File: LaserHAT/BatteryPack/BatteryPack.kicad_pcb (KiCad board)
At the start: 2 copper layers, 100 x 96 mm, 101 parts, among them J1 USB-C PD 20V in, J3 OUT +V/0V/-V + link, J4 LINK from lower pack, Q1 AO3401A, Q10 AO3400A, Q2 AO3401A, Q3 AO3400A, Q4 AO3401A, Q5 AO3400A, Q6 AO3401A, Q7 AO3400A, Q8 AO3400A, Q9 AO3400A, SW1 MTS-203 RUN/OFF/CHG, U1 LM393DR2G, U2 LM393DR2G, U3 CJ431, U4 CH224A, U5 CN3704, U6 HY2213-BB3A, U7 HY2213-BB3A, U8 HY2213-BB3A, U9 HY2213-BB3A

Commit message: BatteryPack: all four cells the same way round, 4 mm polarity marks under each cell
The cells alternated direction in the first routing (short series links);
the user prefers one orientation to avoid insertion errors.  tools/place.py
now puts the - clip (odd BCn) on the left and the + clip on the right in all
four rows and draws 4 mm "-" / "+" silk strokes under each cell body, in
addition to the small marks beside the clips.  The cell-area copper (C1-C3,
GND and +BAT west of the strip) was ripped up and rerouted with Freerouting;
the electronics strip kept its routing.  DRC 0 violations / 0 unconnected,
path_check / sync_check 0; fab outputs and renders regenerated.

Co-Authored-By: Claude Fable 5.1 <noreply@anthropic.com>
Claude-Session: https://claude.ai/code/session_018vgLizGzYPynnY93ajvoVA
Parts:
- moved BC1 48.0 mm to (11.0, 17.0), turned to 0 degrees
- moved BC2 48.0 mm to (59.0, 17.0), turned to 180 degrees
- moved BC5 48.0 mm to (11.0, 57.0), turned to 0 degrees
- moved BC6 48.0 mm to (59.0, 57.0), turned to 180 degrees
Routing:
- net GND: track 283.1 -> 358.7 mm
- net /C2: track 104.3 -> 145.3 mm, vias 2 -> 3
- net /C1: track 124.2 -> 162.1 mm
- net /C3: track 113.6 -> 129.4 mm
- net +BAT: track 166.9 -> 164.9 mm

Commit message: BatteryPack: LCSC codes on the board footprints, JLC model strings as values
A BOM made from the PCB with the Fabrication Toolkit had no part numbers,
because the footprints carried none; JLC then matched by Comment and failed on
the parts with descriptive values (C5, F1, J1, J3, J4, SW1).

- sch_engine.py writes the code into every symbol as "LCSC Part #" (the field
  the Fabrication Toolkit reads) instead of "LCSC"; mounting holes are out of
  the BOM
- new tools/stamp_fields.py stamps the same field (hidden, F.Fab) into every
  footprint, syncs the Values and excludes H1-H4 from BOM and position files
- values of the toggle, PTC, LEDs, USB-C, PH-4 headers, inductor and NTC are
  now JLC's model strings so the Comment matches; J3/J4 roles noted as text
- schematic regenerated (netcheck OK, ERC 0), path/sync checks 0, DRC 0/0,
  fab outputs and PDF regenerated; all codes verified against JLC (toggle
  stock 192)

Co-Authored-By: Claude Fable 5.1 <noreply@anthropic.com>
Claude-Session: https://claude.ai/code/session_018vgLizGzYPynnY93ajvoVA
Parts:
- D1: value red ON -> KT-0603R
- D10: value green DONE -> KT-0805G
- D2: value yellow >20% -> KT-0805Y
- D3: value green >50% -> KT-0805G
- D4: value green >80% -> KT-0805G
- D9: value red CHRG -> KT-0603R
- F1: value 100mA PTC -> MF-MSMF010-2
- J1: value USB-C PD 20V in -> TYPE-C-31-M-12
- J3: value OUT +V/0V/-V + link -> B4B-PH-K-S(LF)(SN)
- J4: value LINK from lower pack -> B4B-PH-K-S(LF)(SN)
- L1: value 22uH 3A -> MWSA0603S-220MT
- RT1: value NTC 10k -> NCP18XH103F03RB
- SW1: value MTS-203 RUN/OFF/CHG -> CAX-MTS203M-YB-10.6JL

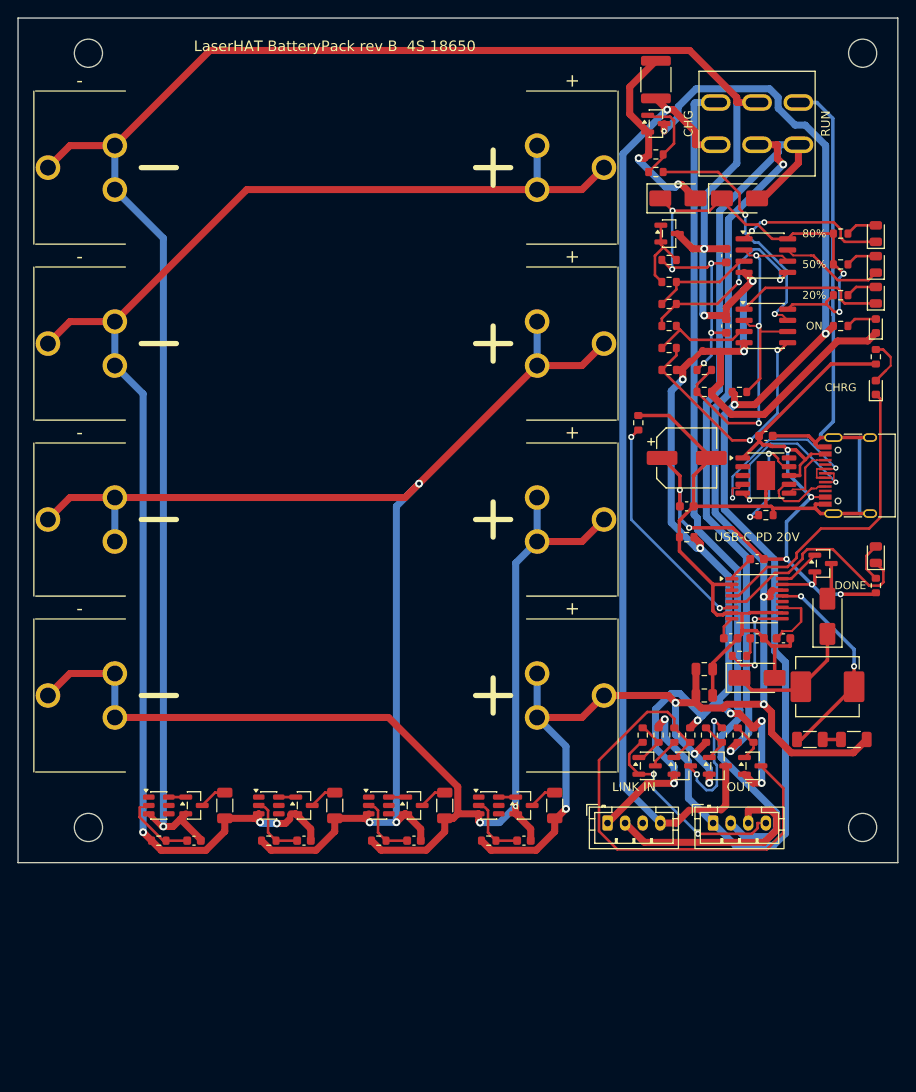
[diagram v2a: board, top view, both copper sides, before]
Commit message: BatteryPack: 100 x 120 mm, switch between the headers and the charger, balancers beside their cells
Re-placed and rerouted at the user's request (shorter power runs, no long
traces to the switch):

- board 100 x 120 mm, holes at (8|96, 4|116)
- cells all the same way round, + (button) left / - right, 4 mm silk marks;
  the right clips then carry GND, C1, C2, C3 so balancers 1-3 sit in the
  right column between the two clips they tap; balancer 4 bottom left by the
  +BAT clip
- toggle at the bottom centre between J4 LINK IN / J3 OUT and the fuse,
  cutoff and gauge-rail diodes; slave enable above the headers; USB-C on the
  right edge at y 86, charger bottom right; reference, comparators and LEDs
  above the charger with each LED beside its comparator
- new tools/autoroute.py: rip-up, pre-routed stubs out of SMD pads narrower
  than their net class (clipped clear of other pads), Freerouting headless
  (DSN/SES), pruning of unused stubs, DRC summary; route/ is git-ignored
- DRC 0 violations / 0 warnings / 0 unconnected, path_check / sync_check 0,
  fab outputs and renders regenerated

Co-Authored-By: Claude Fable 5.1 <noreply@anthropic.com>
Claude-Session: https://claude.ai/code/session_018vgLizGzYPynnY93ajvoVA
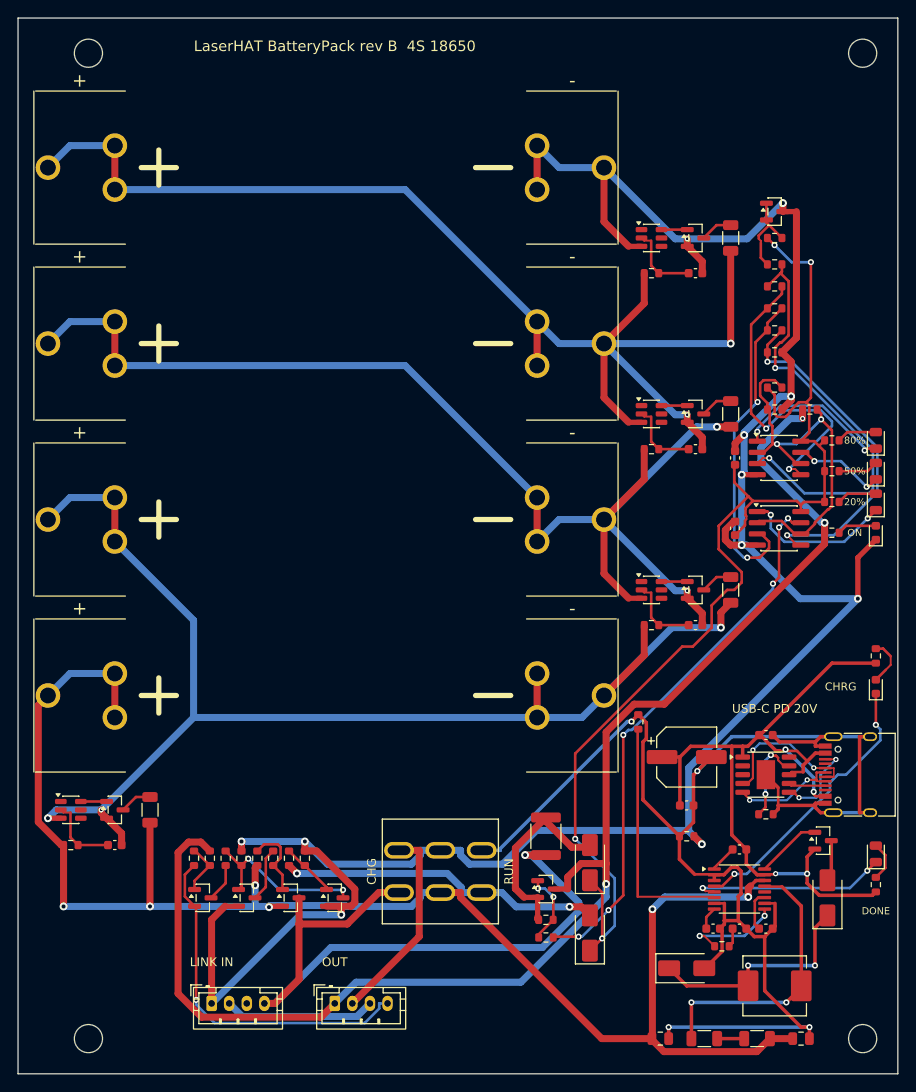
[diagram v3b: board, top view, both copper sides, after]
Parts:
- moved SW1 92.3 mm to (48.0, 97.0)
- moved Q1 87.9 mm to (60.0, 99.0)
- moved R1 87.9 mm to (60.0, 102.5)
- moved R2 87.9 mm to (60.0, 104.5)
- moved F1 86.9 mm to (60.0, 93.0)
- moved R35 86.4 mm to (81.0, 25.0)
- moved C12 86.1 mm to (77.0, 29.0)
- moved Q7 86.1 mm to (77.0, 25.0)
- moved R31 85.4 mm to (72.0, 29.0)
- moved U6 85.4 mm to (72.0, 25.0)
- moved D6 85.2 mm to (65.0, 104.0), turned to 90 degrees
- moved D5 76.2 mm to (65.0, 96.0), turned to 90 degrees
- moved R36 63.3 mm to (81.0, 45.0)
- moved C13 62.9 mm to (77.0, 49.0)
- moved Q8 62.9 mm to (77.0, 45.0)
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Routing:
- net GND: track 358.7 -> 276.5 mm, vias 12 -> 11
- net /OUT_GND: track 96.8 -> 22.9 mm
- net +G: track 69.9 -> 137.2 mm, vias 7 -> 4
- net +CHG: track 87.2 -> 36.9 mm, vias 1 -> 2
- net /TH80: track 11.9 -> 49.7 mm, vias 0 -> 2
- net /EN_G: track 56.5 -> 19.6 mm, vias 0 -> 2
- net /CUT_OC: track 28.2 -> 62.5 mm, vias 2 -> 6
- net +RUN: track 107.5 -> 79.0 mm
- net /TH20: track 11.7 -> 37.0 mm, vias 0 -> 2
- net CGND: track 156.8 -> 179.2 mm, vias 0 -> 4
- net /C3: track 129.4 -> 147.4 mm, vias 2 -> 3
- net +OUT: track 140.5 -> 157.6 mm, vias 4 -> 3
- net /C1: track 162.1 -> 145.3 mm, vias 3 -> 2
- net /STACK_IN: track 24.0 -> 40.7 mm, vias 2 -> 1
- net /TH50: track 22.1 -> 36.2 mm
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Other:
- board size 100 x 96 mm -> 100 x 120 mm

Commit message: BatteryPack rev C: two hobby 4S packs on one 100 x 100 board, one charger, one toggle
Pack sockets J5/J6 (JST-XH right-angle) replace the 18650 clips; packs strap under the board.
Pole 1 of the toggle puts the packs in series (RUN) or joins their negatives (CHARGE); pole 2
runs pack B's output chain or joins the positives through a 1.1 A PTC so one CN3704 charges
both in parallel.  N-FET cutoff in pack A's negative, second gauge, VBUS switch so the charger
only sees the brick in CHARGE.  No stack cable or slave enable.  autoroute.py runs each board
edit in its own process; place.py adds keep-outs round the slots.  DRC 0/0/0, checks clean.

Co-Authored-By: Claude Fable 5.1 <noreply@anthropic.com>
Claude-Session: https://claude.ai/code/session_018vgLizGzYPynnY93ajvoVA
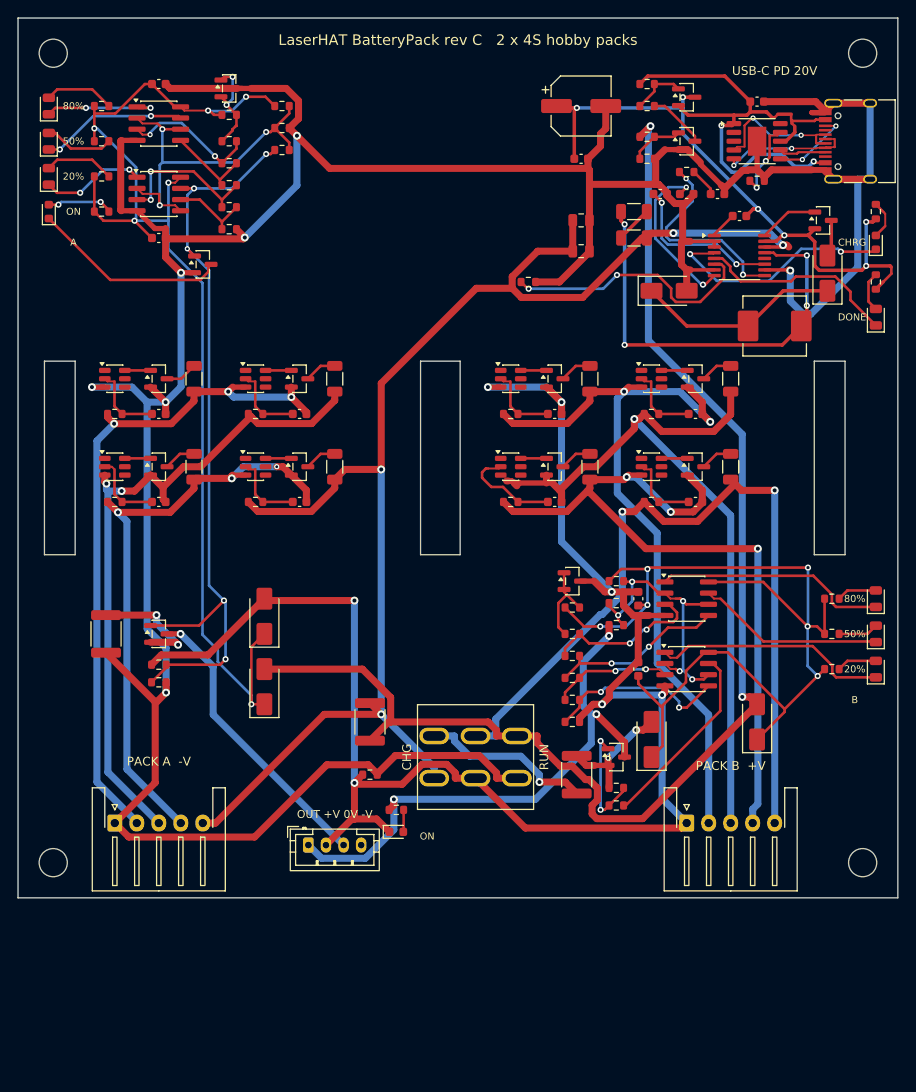
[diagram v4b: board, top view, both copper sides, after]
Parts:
- removed BC1, BC2, BC3, BC4, BC5, BC6, BC7, BC8: MY-18650-01, battpack:Clip_MY-18650-01
- removed J4: B4B-PH-K-S(LF)(SN), Connector_JST:JST_PH_B4B-PH-K_1x04_P2.00mm_Vertical
- removed Q2, Q4: AO3401A, Package_TO_SOT_SMD:SOT-23
- removed Q3, Q5: AO3400A, Package_TO_SOT_SMD:SOT-23
- removed R16, R17, R18, R20, R21, R22, R23: 100k, Resistor_SMD:R_0603_1608Metric
- removed R19: 33k, Resistor_SMD:R_0603_1608Metric
- added C16: 100n, Capacitor_SMD:C_0603_1608Metric, F.Cu at (61.0, 45.0)
- added C17: 100n, Capacitor_SMD:C_0603_1608Metric, F.Cu at (77.0, 45.0)
- added C18: 100n, Capacitor_SMD:C_0603_1608Metric, F.Cu at (61.0, 55.0)
- added C19: 100n, Capacitor_SMD:C_0603_1608Metric, F.Cu at (77.0, 55.0)
- added C20: 100n, Capacitor_SMD:C_0603_1608Metric, F.Cu at (70.5, 66.0)
- added C21: 100n, Capacitor_SMD:C_0603_1608Metric, F.Cu at (70.5, 74.0)
- added D11: KT-0603R, LED_SMD:LED_0603_1608Metric, F.Cu at (43.0, 92.5)
- added D12: KT-0805Y, LED_SMD:LED_0805_2012Metric, F.Cu at (97.5, 74.0)
- added D13: KT-0805G, LED_SMD:LED_0805_2012Metric, F.Cu at (97.5, 70.0)
- added D14: KT-0805G, LED_SMD:LED_0805_2012Metric, F.Cu at (97.5, 66.0)
- added D15: SS14, Diode_SMD:D_SMA, F.Cu at (28.0, 68.0)
- added D16: SS14, Diode_SMD:D_SMA, F.Cu at (28.0, 76.0)
- added F2: MF-MSMF010-2, Fuse:Fuse_1812_4532Metric, F.Cu at (10.0, 70.0)
- added F3: MF-MSMF110/24X-2, Fuse:Fuse_1812_4532Metric, F.Cu at (40.0, 80.0)
- added J5: S5B-XH-A-1(LF)(SN), Connector_JST:JST_XH_S5B-XH-A-1_1x05_P2.50mm_Horizontal, F.Cu at (11.0, 91.5)
- added J6: S5B-XH-A-1(LF)(SN), Connector_JST:JST_XH_S5B-XH-A-1_1x05_P2.50mm_Horizontal, F.Cu at (76.0, 91.5)
- added Q11: AO3400A, Package_TO_SOT_SMD:SOT-23, F.Cu at (16.0, 70.0)
- added Q12: AO3400A, Package_TO_SOT_SMD:SOT-23, F.Cu at (76.0, 14.0)
- added Q13: AO3401A, Package_TO_SOT_SMD:SOT-23, F.Cu at (76.0, 9.00)
- added Q14: AO3400A, Package_TO_SOT_SMD:SOT-23, F.Cu at (21.0, 28.0)
- added Q15: AO3400A, Package_TO_SOT_SMD:SOT-23, F.Cu at (61.0, 41.0)
- added Q16: AO3400A, Package_TO_SOT_SMD:SOT-23, F.Cu at (77.0, 41.0)
- added Q17: AO3400A, Package_TO_SOT_SMD:SOT-23, F.Cu at (61.0, 51.0)
- added Q18: AO3400A, Package_TO_SOT_SMD:SOT-23, F.Cu at (77.0, 51.0)
- added R39: 100k, Resistor_SMD:R_0603_1608Metric, F.Cu at (16.0, 73.5)
- added R40: 100k, Resistor_SMD:R_0603_1608Metric, F.Cu at (16.0, 75.5)
- added R41: 100k, Resistor_SMD:R_0603_1608Metric, F.Cu at (71.5, 13.5)
- added R42: 100k, Resistor_SMD:R_0603_1608Metric, F.Cu at (71.5, 16.0)
- added R43: 100k, Resistor_SMD:R_0603_1608Metric, F.Cu at (71.5, 7.50)
- added R44: 100k, Resistor_SMD:R_0603_1608Metric, F.Cu at (71.5, 10.0)
- added R45: 6.8k, Resistor_SMD:R_0603_1608Metric, F.Cu at (63.0, 67.0)
- added R46: 6.8k, Resistor_SMD:R_0603_1608Metric, F.Cu at (63.0, 70.0)
- added R47: 2k, Resistor_SMD:R_0603_1608Metric, F.Cu at (63.0, 72.5)
- added R48: 2k, Resistor_SMD:R_0603_1608Metric, F.Cu at (63.0, 75.0)
- added R49: 6.2k, Resistor_SMD:R_0603_1608Metric, F.Cu at (63.0, 77.5)
- added R50: 30k, Resistor_SMD:R_0603_1608Metric, F.Cu at (63.0, 80.0)
- added R51: 68k, Resistor_SMD:R_0603_1608Metric, F.Cu at (68.0, 64.0)
- added R52: 10k, Resistor_SMD:R_0603_1608Metric, F.Cu at (68.0, 66.5)
- added R53: 1M, Resistor_SMD:R_0603_1608Metric, F.Cu at (68.0, 69.0)
- added R54: 13k, Resistor_SMD:R_0603_1608Metric, F.Cu at (43.0, 90.0)
- added R55: 13k, Resistor_SMD:R_0603_1608Metric, F.Cu at (92.5, 74.0)
- added R56: 12k, Resistor_SMD:R_0603_1608Metric, F.Cu at (92.5, 70.0)
- added R57: 12k, Resistor_SMD:R_0603_1608Metric, F.Cu at (92.5, 66.0)
- added R58: 100, Resistor_SMD:R_0603_1608Metric, F.Cu at (56.0, 45.0)
- added R59: 100, Resistor_SMD:R_0603_1608Metric, F.Cu at (72.0, 45.0)
- added R60: 100, Resistor_SMD:R_0603_1608Metric, F.Cu at (56.0, 55.0)
- added R61: 100, Resistor_SMD:R_0603_1608Metric, F.Cu at (72.0, 55.0)
- added R62: 100, Resistor_SMD:R_1206_3216Metric, F.Cu at (65.0, 41.0)
- added R63: 100, Resistor_SMD:R_1206_3216Metric, F.Cu at (81.0, 41.0)
- added R64: 100, Resistor_SMD:R_1206_3216Metric, F.Cu at (65.0, 51.0)
- added R65: 100, Resistor_SMD:R_1206_3216Metric, F.Cu at (81.0, 51.0)
- added U10: HY2213-BB3A, Package_TO_SOT_SMD:SOT-23-6, F.Cu at (56.0, 41.0)
- added U11: HY2213-BB3A, Package_TO_SOT_SMD:SOT-23-6, F.Cu at (72.0, 41.0)
- added U12: HY2213-BB3A, Package_TO_SOT_SMD:SOT-23-6, F.Cu at (56.0, 51.0)
- added U13: HY2213-BB3A, Package_TO_SOT_SMD:SOT-23-6, F.Cu at (72.0, 51.0)
- added U14: LM393DR2G, Package_SO:SOIC-8_3.9x4.9mm_P1.27mm, F.Cu at (76.0, 66.0)
- added U15: LM393DR2G, Package_SO:SOIC-8_3.9x4.9mm_P1.27mm, F.Cu at (76.0, 74.0)
- added U16: CJ431, Package_TO_SOT_SMD:SOT-23, F.Cu at (63.0, 64.0)
- R11: value 1M -> 470k
- moved D4 101.4 mm to (3.50, 10.0)
- moved D3 101.2 mm to (3.50, 14.0)
- moved D2 101.0 mm to (3.50, 18.0)
- moved D1 100.8 mm to (3.50, 22.0)
- moved C7 96.3 mm to (64.0, 23.0)
- moved R25 94.3 mm to (70.0, 22.0)
- moved R26 92.1 mm to (70.0, 25.0)
- moved R15 91.3 mm to (9.50, 10.0)
- moved R14 91.1 mm to (9.50, 14.0)
- moved R13 90.9 mm to (9.50, 18.0)
- moved R12 90.7 mm to (9.50, 22.0)
- moved C8 90.0 mm to (64.0, 26.5)
- moved R27 88.1 mm to (76.0, 17.5)
- moved C11 84.4 mm to (73.0, 20.0)
- moved C9 83.6 mm to (76.0, 20.0)
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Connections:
- C10 pad 2: CGND -> GND
- C11 pad 2: CGND -> GND
- C3 pad 2: CGND -> GND
- C4 pad 2: VBUS -> VCHG
- C5 pad 1: VBUS -> VCHG
- C5 pad 2: CGND -> GND
- C6 pad 1: VBUS -> VCHG
- C6 pad 2: CGND -> GND
- C7 pad 2: CGND -> GND
- C8 pad 2: CGND -> GND
- C9 pad 2: CGND -> GND
- D1 pad 1: GND -> /D1_K
- D5 pad 1: +G -> +GB
- D6 pad 1: +G -> +GB
- D6 pad 2: +CHG -> +CHGB
- D8 pad 2: CGND -> GND
- J1 pad A1: CGND -> GND
- J1 pad A12: CGND -> GND
- J1 pad B1: CGND -> GND
- J1 pad B12: CGND -> GND
- J1 pad S1: CGND -> GND
- J3 pad 2: /OUT_GND -> 0V
- J3 pad 3: /LINK_N -> /-V
- J3 pad 4: /STACK_IN -> unconnected-(J3-Pin_4-Pad4)
- Q6 pad 2: VBUS -> VCHG
- R11 pad 1: +OUT -> /Q11_G
- R12 pad 1: +OUT -> +G
- R2 pad 2: /CUT_OC -> /CUT_OCB
- R24 pad 2: CGND -> GND
- R28 pad 1: VBUS -> VCHG
- R29 pad 1: VBUS -> VCHG
- R30 pad 1: CGND -> 0V
- RT1 pad 2: CGND -> GND
- SW1 pad 1: +RUN -> +BAT
- SW1 pad 2: +BAT -> 0V
- SW1 pad 3: +CHG -> GND
- SW1 pad 4: /OUT_GND -> +RUN
- SW1 pad 5: GND -> +BATB
- SW1 pad 6: CGND -> +CHGB
- U2 pad 5: /THCUT -> /VS
- U2 pad 6: /VS -> /THCUT
- U2 pad 7: /CUT_OC -> /Q11_G
- U4 pad 11: CGND -> GND
- U5 pad 10: CGND -> GND
- U5 pad 15: VBUS -> VCHG
- U5 pad 2: CGND -> GND
- U5 pad 3: CGND -> GND
- U5 pad 7: CGND -> GND
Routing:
- net 0V: track 0.00 -> 195.5 mm, vias 0 -> 7
- net CGND: track 179.2 -> 0.00 mm, vias 4 -> 0
- net +CHGB: track 0.00 -> 149.8 mm, vias 0 -> 2
- net GND: track 276.5 -> 392.3 mm, vias 11 -> 7
- net +GB: track 0.00 -> 114.2 mm, vias 0 -> 6
- net +OUT: track 157.6 -> 63.5 mm
- net +BATB: track 0.00 -> 93.1 mm, vias 0 -> 2
- net /Q11_G: track 0.00 -> 88.5 mm, vias 0 -> 5
- net /B1: track 0.00 -> 88.4 mm, vias 0 -> 2
- net /B2: track 0.00 -> 87.4 mm, vias 0 -> 1
- net /B3: track 0.00 -> 86.5 mm, vias 0 -> 3
- net /C3: track 147.4 -> 68.4 mm
- net VCHG: track 0.00 -> 72.5 mm, vias 0 -> 6
- net /C1: track 145.3 -> 78.0 mm, vias 2 -> 3
- net /CUT_OC: track 62.5 -> 0.00 mm, vias 6 -> 0
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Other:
- board size 100 x 120 mm -> 100 x 100 mm
- board text added: "A"
- board text added: "B"
- board text added: "LaserHAT BatteryPack rev C 2 x 4S hobby packs"
- board text added: "OUT +V 0V -V"
- board text added: "PACK A (-V side, leads to J5)"
- board text added: "PACK A -V"
- board text added: "PACK B (+V side, leads to J6)"
- board text added: "PACK B +V"
- board text removed: "+"
- board text removed: "-"
- board text removed: "LINK IN"
- board text removed: "LaserHAT BatteryPack rev B 4S 18650"
- board text removed: "OUT"

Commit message: BatteryPack rev C: XT60 sockets for the packs' discharge leads, pack B ON LED in its column
J7 / J8 (Amass XT60PW-M, C98732) at the front edge inboard of the XH sockets carry the run and charge
current; the balance leads keep the cell taps (XH pins 1 / 5 parallel the XT60).  Toggle and output
header sit between the XT60s, chain B moved right of its gauge, F3 / R30 above J7.  R54 on +OUT beside
Q1, thin net to D11 at the bottom of pack B's LED column.  Re-routed (Freerouting), stubs pruned,
DRC 0 / 0 / 0, ERC 0, path / sync 0, fab 136 placements / 44 BOM lines.

Co-Authored-By: Claude Fable 5.1 <noreply@anthropic.com>
Claude-Session: https://claude.ai/code/session_018vgLizGzYPynnY93ajvoVA
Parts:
- added J7: XT60PW-M, Connector_AMASS:AMASS_XT60PW-M_1x02_P7.20mm_Horizontal, F.Cu at (36.0, 83.1)
- added J8: XT60PW-M, Connector_AMASS:AMASS_XT60PW-M_1x02_P7.20mm_Horizontal, F.Cu at (69.0, 83.1)
- moved D11 56.4 mm to (97.5, 78.0), turned to 90 degrees
- moved R54 49.2 mm to (87.5, 69.0)
- moved R1 30.5 mm to (87.5, 64.0)
- moved R2 30.2 mm to (87.5, 66.5)
- moved F1 28.7 mm to (83.0, 65.0)
- moved Q1 20.5 mm to (83.0, 70.0)
- moved J3 12.5 mm to (45.5, 94.5)
- moved D5 12.1 mm to (83.0, 77.0)
- moved F3 10.0 mm to (40.0, 70.0)
- moved R30 10.0 mm to (40.0, 76.0)
- moved D6 5.66 mm to (88.0, 76.0)
- moved J6 3.50 mm to (79.5, 91.5)
- moved SW1 3.00 mm to (49.0, 84.0)
- moved R46 1.00 mm to (63.0, 69.0)
- moved R47 1.00 mm to (63.0, 71.5)
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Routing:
- net Net-(U13-VDD): track 8.68 -> 49.8 mm
- net +GB: track 114.2 -> 74.2 mm
- net +OUT: track 63.5 -> 95.1 mm, vias 3 -> 4
- net +RUN: track 19.7 -> 50.7 mm
- net +CHGB: track 149.8 -> 174.0 mm, vias 2 -> 3
- net GND: track 392.3 -> 371.9 mm, vias 7 -> 8
- net /B3: track 86.5 -> 68.8 mm, vias 3 -> 1
- net 0V: track 195.5 -> 212.6 mm, vias 7 -> 8
- net VBUS: track 57.9 -> 41.4 mm, vias 2 -> 4
- net /C2: track 77.2 -> 90.6 mm, vias 2 -> 1
- net /-V: track 33.2 -> 46.2 mm
- net +BATB: track 93.1 -> 104.9 mm, vias 2 -> 1
- net Net-(D11-A): track 2.52 -> 13.3 mm, vias 0 -> 2
- net /CUT_OCB: track 21.7 -> 31.6 mm, vias 0 -> 2
- net /Q11_G: track 88.5 -> 80.0 mm, vias 5 -> 4
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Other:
- board text added: "PACK A (-V side, plugs to J7 / J5)"
- board text added: "PACK B (+V side, plugs to J8 / J6)"
- board text removed: "PACK A (-V side, leads to J5)"
- board text removed: "PACK B (+V side, leads to J6)"

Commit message: BatteryPack: 3D model for the XT60PW-M sockets
KiCad 9 ships no model for the horizontal XT60, so battpack.pretty/XT60PW-M.kicad_mod is KiCad's AMASS footprint
pointed at battpack.3dshapes/XT60PW-M.step, built by tools/make_xt60_model.py (CadQuery) from the vertical XT60-M
nose plus the PW body, bent pins and legs after Amass drawing XT60PW-M30.  Board swapped in place (copper kept),
DRC 0 / 0 / 0, path / sync 0; renders show the sockets.

Co-Authored-By: Claude Fable 5.1 <noreply@anthropic.com>
Claude-Session: https://claude.ai/code/session_018vgLizGzYPynnY93ajvoVA
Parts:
- J7, J8: footprint Connector_AMASS:AMASS_XT60PW-M_1x02_P7.20mm_Horizontal -> battpack:XT60PW-M
